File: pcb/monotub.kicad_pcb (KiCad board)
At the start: 2 copper layers, 36 parts, among them J1 HV1, J2 RGB, J3 PROG, J4 SCD-40, J5 WLVL, J9 HV2, Q1 NMOS, Q2 NMOS, Q3 NMOS, SW1 RST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

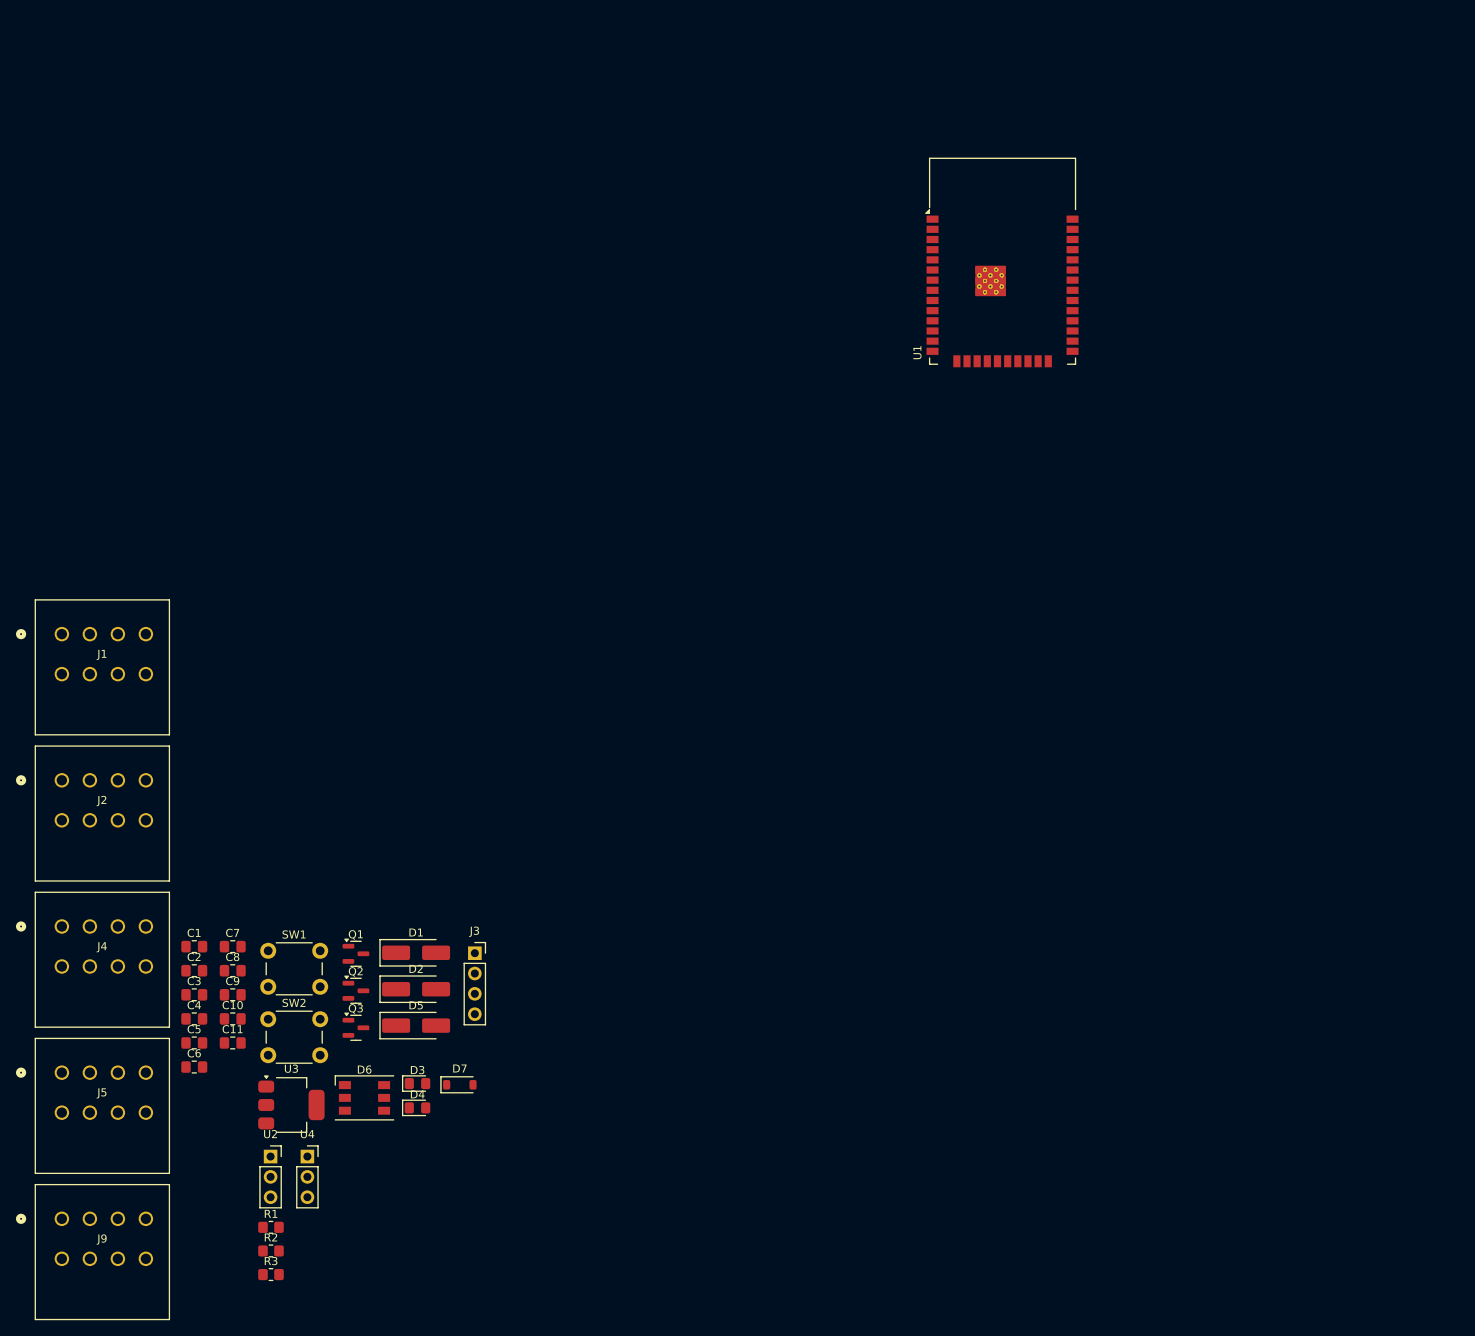
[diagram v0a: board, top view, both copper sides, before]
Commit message: Update board with logo and place all components
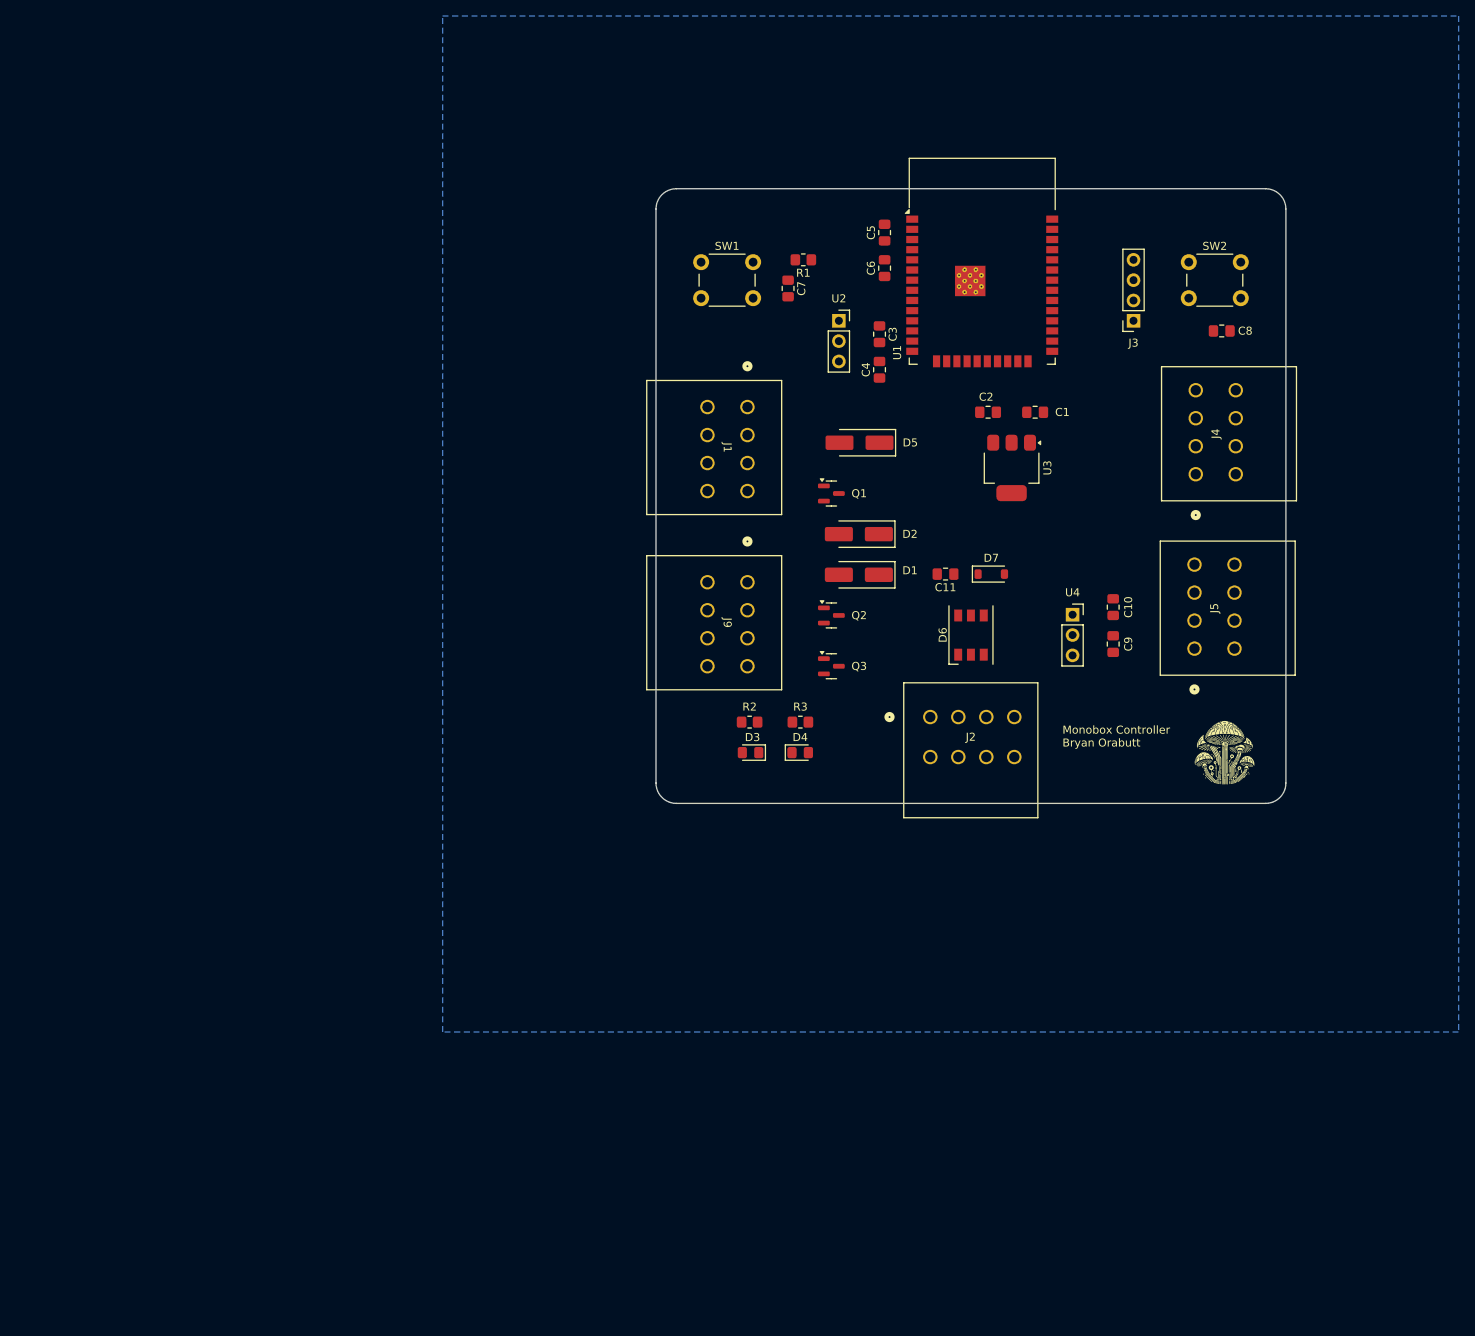
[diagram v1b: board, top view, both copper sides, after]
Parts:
- added G***: LOGO, pcb:logo_inverted_small, F.Cu at (174.0, 117.5)
- added G***: LOGO, pcb:logo_inverted, B.Cu at (142.2, 86.4)
- moved J4 152.6 mm to (170.3, 82.7), turned to 90 degrees
- moved J5 151.2 mm to (170.2, 104.5), turned to 90 degrees
- moved SW2 149.0 mm to (169.5, 56.2)
- moved C8 147.2 mm to (173.6, 64.8)
- moved R1 138.0 mm to (121.3, 55.9), turned to 180 degrees
- moved C5 133.1 mm to (131.4, 52.5), turned to 90 degrees
- moved C6 132.0 mm to (131.4, 56.9), turned to 90 degrees
- moved U2 126.3 mm to (125.7, 63.5)
- moved C1 124.5 mm to (150.3, 74.9), turned to 180 degrees
- moved C10 121.5 mm to (160.0, 99.3), turned to -90 degrees
- moved C2 121.3 mm to (144.4, 74.9)
- moved U3 120.2 mm to (147.3, 81.9), turned to -90 degrees
- moved C3 119.0 mm to (130.8, 65.2), turned to -90 degrees
- moved C9 118.5 mm to (160.0, 103.9), turned to 90 degrees
- moved C4 118.0 mm to (130.8, 69.6), turned to 90 degrees
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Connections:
- net Net-(D6-VCC) renamed /vdd_led
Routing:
- added copper zone on B.Cu, net GND
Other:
- board outline added: 78.7 x 76.8 mm
- board text added: "Monobox Controller Bryan Orabutt"

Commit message: Update PCB routing.
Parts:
- moved J3 49.1 mm to (114.9, 51.4), turned to -90 degrees
- moved C6 5.68 mm to (127.6, 52.7)
- moved C8 4.04 mm to (169.5, 64.8)
- moved SW1 3.24 mm to (107.9, 59.3)
- moved C7 3.24 mm to (118.7, 62.6)
- moved R1 3.24 mm to (120.7, 59.1)
- moved C5 0.23 mm to (131.4, 52.7)
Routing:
- net +3.3V: track 0.00 -> 231.9 mm
- net +24V: track 0.00 -> 159.3 mm
- net GND: track 0.00 -> 120.2 mm, vias 0 -> 17
- net /SCL: track 0.00 -> 100.7 mm
- net /SDA: track 0.00 -> 90.2 mm
- net /RGB: track 0.00 -> 64.2 mm, vias 0 -> 2
- net +5V_LED: track 0.00 -> 49.1 mm
- net /TX: track 0.00 -> 46.3 mm, vias 0 -> 1
- net /RX: track 0.00 -> 44.0 mm, vias 0 -> 1
- net Net-(U1-IO0): track 0.00 -> 36.7 mm
- net +5V: track 0.00 -> 34.8 mm
- net /RST: track 0.00 -> 34.4 mm
- net Net-(D6-DOUT): track 0.00 -> 27.7 mm
- net /FAN_OUT: track 0.00 -> 21.0 mm
- net /HUMID_OUT: track 0.00 -> 19.6 mm
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- added copper zone on F.Cu, net GND

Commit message: Finish routing the board
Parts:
- added REF**: MountingHole_3.2mm_M3, MountingHole:MountingHole_3.2mm_M3, F.Cu at (107.3, 51.4)
- added REF**: MountingHole_3.2mm_M3, MountingHole:MountingHole_3.2mm_M3, F.Cu at (107.3, 119.4)
- added REF**: MountingHole_3.2mm_M3, MountingHole:MountingHole_3.2mm_M3, F.Cu at (177.2, 51.4)
- added REF**: MountingHole_3.2mm_M3, MountingHole:MountingHole_3.2mm_M3, F.Cu at (177.2, 119.4)
- moved J3 6.84 mm to (121.3, 54.0)
- moved G*** 4.62 mm to (169.5, 118.7)
- moved C8 4.12 mm to (166.3, 67.3)
- moved BOOT 4.12 mm to (166.2, 58.7)
- renumbered SW2 to BOOT, SW1 to RST
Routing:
- net /PUMP: track 0.00 -> 86.3 mm, vias 0 -> 2
- net /HUMID: track 0.00 -> 58.2 mm, vias 0 -> 2
- net /LED: track 0.00 -> 58.1 mm, vias 0 -> 2
- net GND: track 120.2 -> 66.0 mm, vias 17 -> 18
- net /FAN: track 0.00 -> 46.1 mm, vias 0 -> 2
- net /PUMP_OUT: track 14.9 -> 33.4 mm
- net +3.3V: track 231.9 -> 223.5 mm
- net /TX: track 46.3 -> 40.0 mm, vias 1 -> 0
- net /RX: track 44.0 -> 37.8 mm, vias 1 -> 0
- net Net-(U1-IO0): track 36.7 -> 30.7 mm
- net /SDA: track 90.2 -> 86.6 mm
- net /SCL: track 100.7 -> 97.6 mm
- net +24V: track 159.3 -> 161.6 mm
